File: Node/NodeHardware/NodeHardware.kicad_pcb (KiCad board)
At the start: 2 copper layers, 100 x 100 mm, 83 parts, among them J1 USB_C_Receptacle_USB2.0_16P, Q1 AO3401A, Q2 AO3401A, U1 TPS565201DDCR, U2 TPS565201DDCR, U3 CH340C, U4 TLV70433DBVR, U5 MCP73831-2-OT, U6 UCC27511ADBV, U7 ESP32-S3-WROOM-1

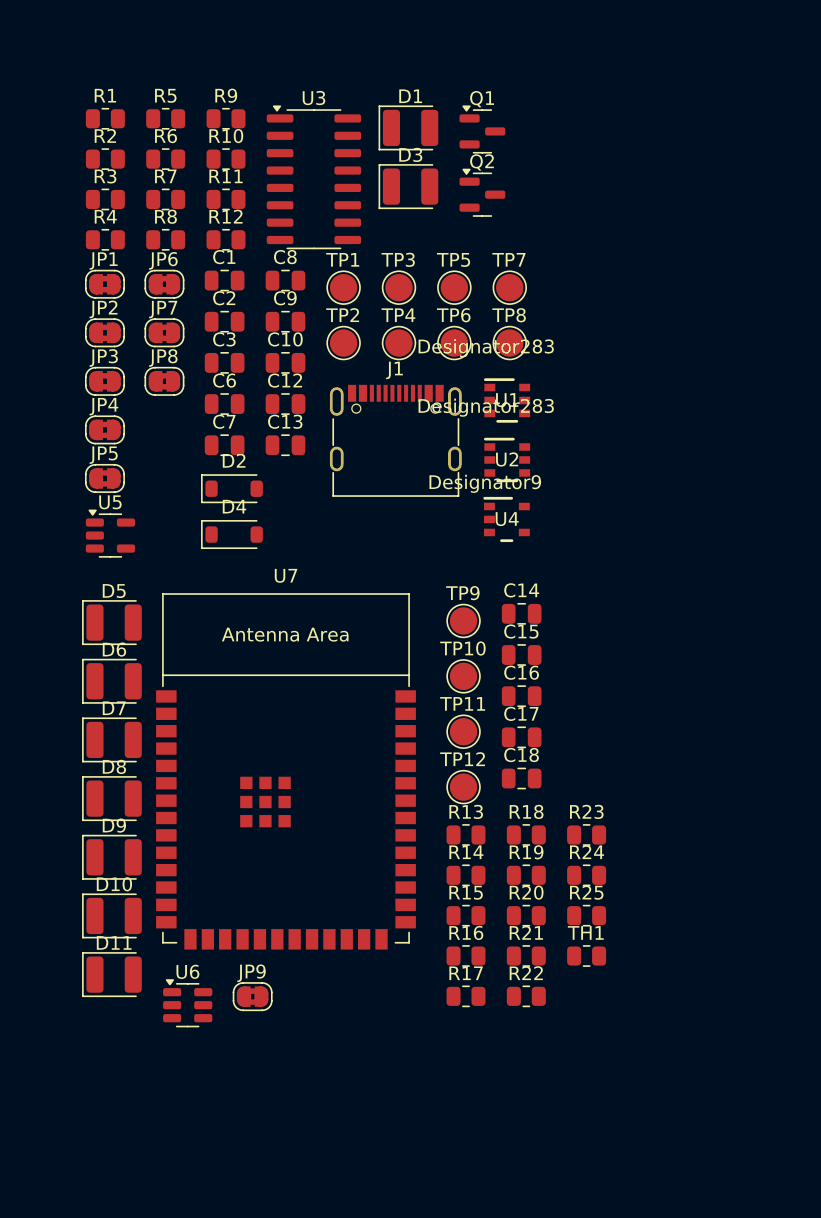
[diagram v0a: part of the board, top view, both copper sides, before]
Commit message: Finish all the basic SCHM needed for the ESP32
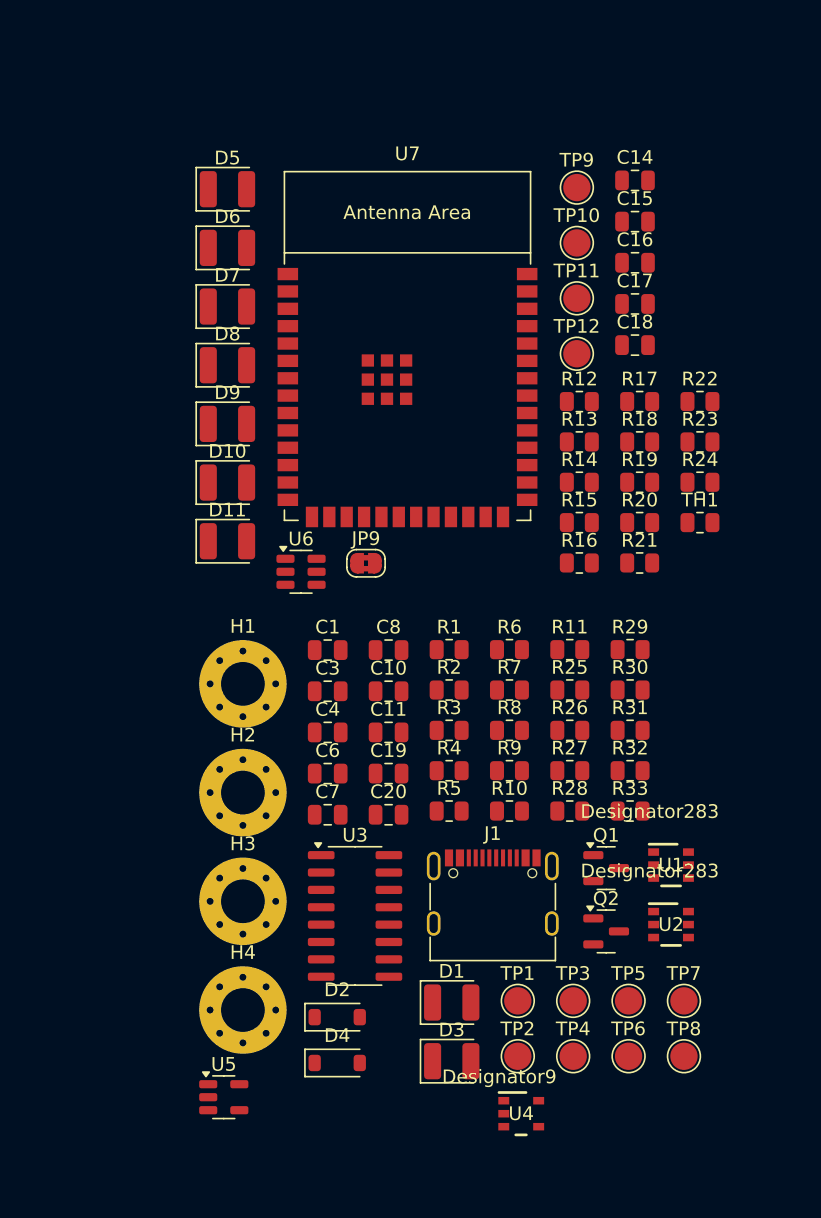
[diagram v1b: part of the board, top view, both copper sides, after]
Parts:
- removed C12, C13, C2, C9: C, Capacitor_SMD:C_0805_2012Metric
- removed JP1, JP2, JP3, JP4, JP5, JP6, JP7, JP8: SolderJumper_2_Bridged, Jumper:SolderJumper-2_P1.3mm_Bridged2Bar_RoundedPad1.0x1.5mm
- added C11: 1u, Capacitor_SMD:C_0805_2012Metric, F.Cu at (144.9, 104.5)
- added C19: 1u, Capacitor_SMD:C_0805_2012Metric, F.Cu at (144.9, 107.5)
- added C20: 100n, Capacitor_SMD:C_0805_2012Metric, F.Cu at (144.9, 110.5)
- added C4: 1u, Capacitor_SMD:C_0805_2012Metric, F.Cu at (140.4, 104.5)
- added H1: MountingHole, MountingHole:MountingHole_3.2mm_M3_Pad_Via, F.Cu at (134.2, 101.0)
- added H2: MountingHole, MountingHole:MountingHole_3.2mm_M3_Pad_Via, F.Cu at (134.2, 108.9)
- added H3: MountingHole, MountingHole:MountingHole_3.2mm_M3_Pad_Via, F.Cu at (134.2, 116.9)
- added H4: MountingHole, MountingHole:MountingHole_3.2mm_M3_Pad_Via, F.Cu at (134.2, 124.8)
- added R26: 0R, Resistor_SMD:R_0805_2012Metric, F.Cu at (158.2, 104.4)
- added R27: 4k7, Resistor_SMD:R_0805_2012Metric, F.Cu at (158.2, 107.3)
- added R28: 0R, Resistor_SMD:R_0805_2012Metric, F.Cu at (158.2, 110.3)
- added R29: 10k, Resistor_SMD:R_0805_2012Metric, F.Cu at (162.6, 98.5)
- added R30: 0R, Resistor_SMD:R_0805_2012Metric, F.Cu at (162.6, 101.4)
- added R31: 0R, Resistor_SMD:R_0805_2012Metric, F.Cu at (162.6, 104.4)
- added R32: 0R, Resistor_SMD:R_0805_2012Metric, F.Cu at (162.6, 107.3)
- added R33: 0R, Resistor_SMD:R_0805_2012Metric, F.Cu at (162.6, 110.3)
- C1, C8: value C -> 100n
- C10, C3, C6: value C -> 10u
- C7: value C -> 1u
- J1: value USB_C_Receptacle_USB2.0_16P -> USB_C_Receptacle_16P
- R1, R4, R9: value R -> 10k
- R10, R11: value R -> 5k1
- R12, R13, R14, R15, R16, R17, R18, R19, R20, R21, R22, R23, R24, R5, R8: value R -> 47k
- R2: value R -> 54.9k
- R25, R3: value R -> 0R
- R6: value R -> ???
- R7: value R -> 4k7
- TP1: value TestPoint -> 5V_TP
- TP2: value TestPoint -> V_IN_TP
- TP3: value TestPoint -> GND_TP_1
- TP4: value TestPoint -> GND_TP_2
- TP5: value TestPoint -> GND_TP_3
- TP6: value TestPoint -> GND_TP_4
- TP7: value TestPoint -> 3V3_TP
- moved D3 64.0 mm to (149.5, 128.6)
- moved D1 64.0 mm to (149.5, 124.3)
- moved R5 54.7 mm to (149.3, 110.3)
- moved Q1 54.6 mm to (160.8, 114.4)
- moved Q2 54.6 mm to (160.8, 119.1)
- moved U3 54.0 mm to (142.4, 117.9)
- moved TP3 53.7 mm to (158.4, 124.2)
- moved TP7 53.7 mm to (166.5, 124.2)
- moved TP1 53.7 mm to (154.3, 124.2)
- moved TP5 53.7 mm to (162.4, 124.2)
- moved TP2 53.7 mm to (154.3, 128.2)
- moved TP4 53.7 mm to (158.4, 128.2)
- moved TP6 53.7 mm to (162.4, 128.2)
- moved TP8 53.7 mm to (166.5, 128.2)
- moved R10 52.0 mm to (153.7, 110.3)
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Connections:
- net Net-(J1-D+-PadA6) renamed USB_D+
- net Net-(J1-D--PadA7) renamed USB_D-
- C1 pad 1: unconnected-(C1-Pad1) -> /5V_REG_SW
- C1 pad 2: unconnected-(C1-Pad2) -> Net-(U1-VBST)
- C10 pad 1: unconnected-(C10-Pad1) -> +3.3V
- C10 pad 2: unconnected-(C10-Pad2) -> PWR_IN_N
- C14 pad 1: GND -> PWR_IN_N
- C15 pad 1: GND -> PWR_IN_N
- C16 pad 1: GND -> PWR_IN_N
- C3 pad 1: unconnected-(C3-Pad1) -> +5V
- C3 pad 2: unconnected-(C3-Pad2) -> PWR_IN_N
- C6 pad 1: unconnected-(C6-Pad1) -> V_IN
- C6 pad 2: unconnected-(C6-Pad2) -> PWR_IN_N
- C7 pad 1: unconnected-(C7-Pad1) -> V_IN
- C7 pad 2: unconnected-(C7-Pad2) -> PWR_IN_N
- C8 pad 1: unconnected-(C8-Pad1) -> /3V3_REG_SW
- C8 pad 2: unconnected-(C8-Pad2) -> Net-(U2-VBST)
- D1 pad 1: unconnected-(D1-K-Pad1) -> /5V_REG_LED_K
- D1 pad 2: unconnected-(D1-A-Pad2) -> +5V
- D2 pad 1: unconnected-(D2-K-Pad1) -> V_IN
- D2 pad 2: unconnected-(D2-A-Pad2) -> /PWR_IN_ZENER
- D3 pad 1: unconnected-(D3-K-Pad1) -> /3V3_REG_LED_K
- D3 pad 2: unconnected-(D3-A-Pad2) -> +3.3V
- J1 pad A1: Net-(J1-GND-PadA1) -> PWR_IN_N
- J1 pad A12: Net-(J1-GND-PadA1) -> PWR_IN_N
- J1 pad A4: Net-(J1-VBUS-PadA4) -> VBUS
- J1 pad A5: unconnected-(J1-CC1-PadA5) -> Net-(J1-CC1)
- J1 pad A9: Net-(J1-VBUS-PadA4) -> VBUS
- J1 pad B1: Net-(J1-GND-PadA1) -> PWR_IN_N
- J1 pad B12: Net-(J1-GND-PadA1) -> PWR_IN_N
- J1 pad B4: Net-(J1-VBUS-PadA4) -> VBUS
- J1 pad B5: unconnected-(J1-CC2-PadB5) -> Net-(J1-CC2)
- J1 pad B9: Net-(J1-VBUS-PadA4) -> VBUS
- Q1 pad 1: unconnected-(Q1-G-Pad1) -> /PWR_IN_ZENER
- Q1 pad 2: unconnected-(Q1-S-Pad2) -> V_IN
- Q1 pad 3: unconnected-(Q1-D-Pad3) -> PWR_IN_P
- R1 pad 1: unconnected-(R1-Pad1) -> /5V_REG_IN
- R1 pad 2: unconnected-(R1-Pad2) -> 5V_REG_EN
- R10 pad 1: unconnected-(R10-Pad1) -> Net-(J1-CC1)
- R10 pad 2: unconnected-(R10-Pad2) -> PWR_IN_N
- R11 pad 1: unconnected-(R11-Pad1) -> Net-(J1-CC2)
- R11 pad 2: unconnected-(R11-Pad2) -> PWR_IN_N
- R13 pad 1: +BATT -> +3.3V
- R14 pad 1: +3.3V -> +BATT
- R16 pad 1: Net-(R13-Pad2) -> Net-(R14-Pad2)
- R16 pad 2: GND -> PWR_IN_N
- R2 pad 1: unconnected-(R2-Pad1) -> +5V
- R2 pad 2: unconnected-(R2-Pad2) -> /5V_REG_VFB
- R25 pad 1: unconnected-(R25-Pad1) -> +5V
- R25 pad 2: unconnected-(R25-Pad2) -> /3V3_REG_IN
- R3 pad 1: unconnected-(R3-Pad1) -> VBUS
- R3 pad 2: unconnected-(R3-Pad2) -> +5V
- R4 pad 1: unconnected-(R4-Pad1) -> /5V_REG_VFB
- R4 pad 2: unconnected-(R4-Pad2) -> PWR_IN_N
- R5 pad 1: unconnected-(R5-Pad1) -> /PWR_IN_ZENER
- R5 pad 2: unconnected-(R5-Pad2) -> PWR_IN_N
- R6 pad 1: unconnected-(R6-Pad1) -> +3.3V
- R6 pad 2: unconnected-(R6-Pad2) -> /3V3_REG_VFB
- R7 pad 1: unconnected-(R7-Pad1) -> /3V3_REG_LED_K
- R7 pad 2: unconnected-(R7-Pad2) -> PWR_IN_N
- R9 pad 1: unconnected-(R9-Pad1) -> /3V3_REG_VFB
- R9 pad 2: unconnected-(R9-Pad2) -> PWR_IN_N
- TH1 pad 1: Net-(R14-Pad2) -> Net-(R13-Pad2)
- TH1 pad 2: GND -> PWR_IN_N
- TP1 pad 1: unconnected-(TP1-Pad1) -> +5V
- TP2 pad 1: unconnected-(TP2-Pad1) -> V_IN
- TP3 pad 1: unconnected-(TP3-Pad1) -> PWR_IN_N
- TP4 pad 1: unconnected-(TP4-Pad1) -> PWR_IN_N
- TP5 pad 1: unconnected-(TP5-Pad1) -> PWR_IN_N
- TP6 pad 1: unconnected-(TP6-Pad1) -> PWR_IN_N
- TP7 pad 1: unconnected-(TP7-Pad1) -> +3.3V
- U1 pad 1: unconnected-(U1-GND-Pad1) -> PWR_IN_N
- U1 pad 2: unconnected-(U1-SW-Pad2) -> /5V_REG_SW
- U1 pad 3: unconnected-(U1-VIN-Pad3) -> /5V_REG_IN
- U1 pad 4: unconnected-(U1-VFB-Pad4) -> /5V_REG_VFB
- U1 pad 5: unconnected-(U1-EN-Pad5) -> 5V_REG_EN
- U1 pad 6: unconnected-(U1-VBST-Pad6) -> Net-(U1-VBST)
- U2 pad 1: unconnected-(U2-GND-Pad1) -> PWR_IN_N
- U2 pad 2: unconnected-(U2-SW-Pad2) -> /3V3_REG_SW
- U2 pad 3: unconnected-(U2-VIN-Pad3) -> /3V3_REG_IN
- U2 pad 4: unconnected-(U2-VFB-Pad4) -> /3V3_REG_VFB
- U2 pad 5: unconnected-(U2-EN-Pad5) -> 3V3_REG_EN
- U2 pad 6: unconnected-(U2-VBST-Pad6) -> Net-(U2-VBST)
- U3 pad 1: unconnected-(U3-GND-Pad1) -> PWR_IN_N
- U3 pad 5: unconnected-(U3-UD+-Pad5) -> /CH340_USB_D+
- U3 pad 6: unconnected-(U3-UD--Pad6) -> /CH340_USB_D-
- U7 pad 1: GND -> PWR_IN_N
- U7 pad 40: GND -> PWR_IN_N
- U7 pad 41: GND -> PWR_IN_N

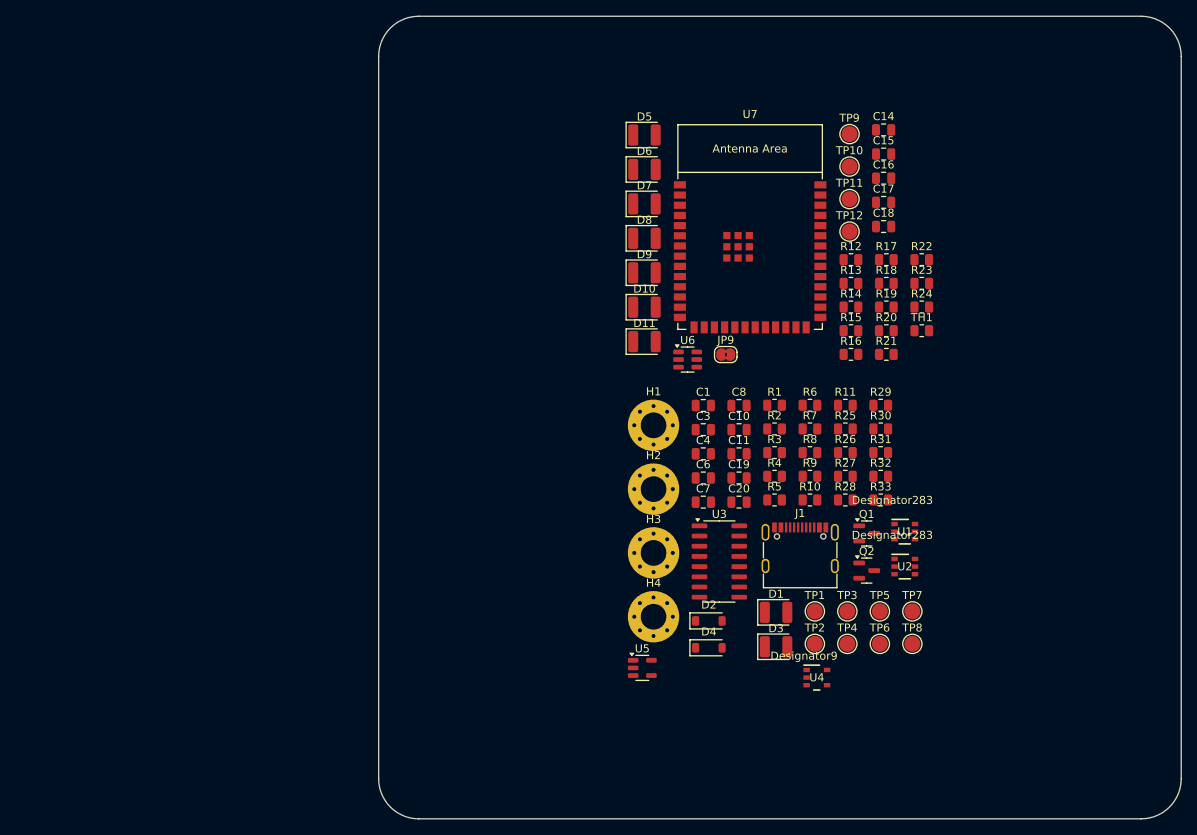
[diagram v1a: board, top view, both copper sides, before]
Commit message: added some comments and sim module to schematic
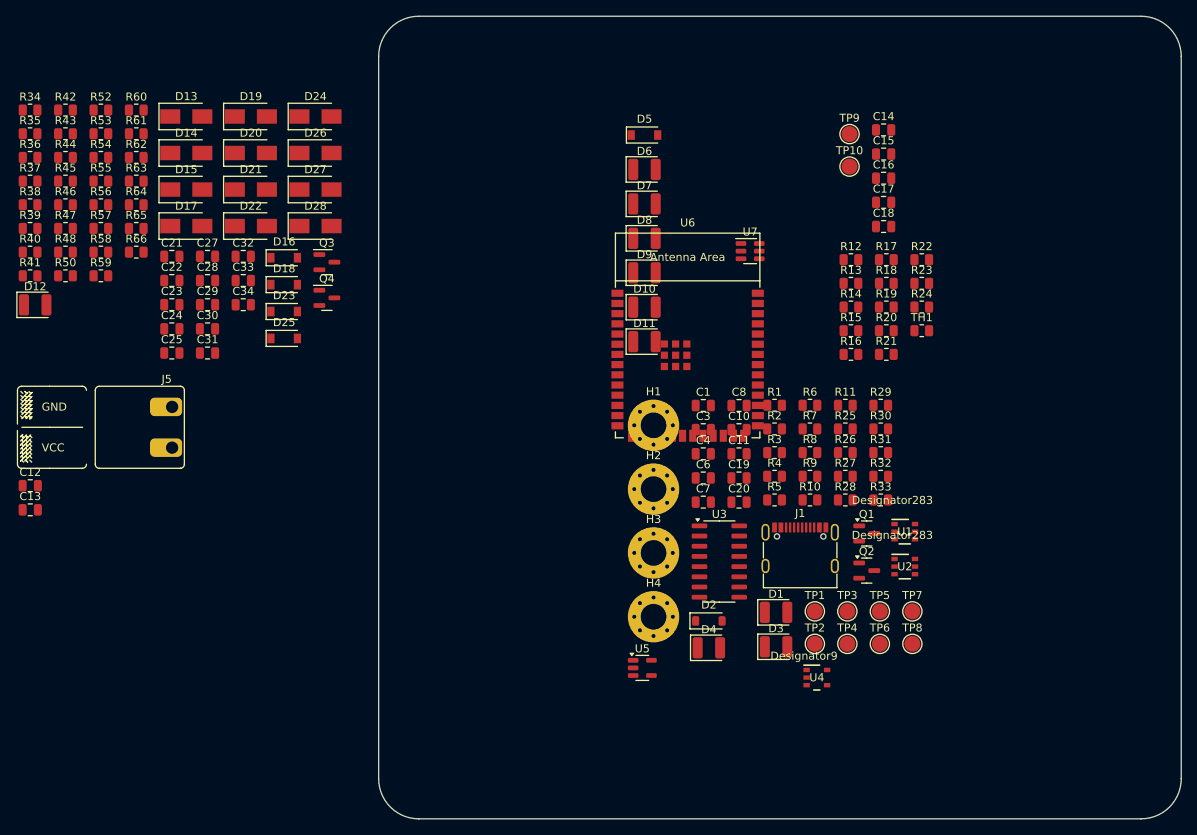
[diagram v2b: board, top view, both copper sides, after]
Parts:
- removed JP9: SolderJumper_2_Bridged, Jumper:SolderJumper-2_P1.3mm_Bridged2Bar_RoundedPad1.0x1.5mm
- removed TP11, TP12: TestPoint, TestPoint:TestPoint_Pad_D2.0mm
- added C12: 100n, Capacitor_SMD:C_0805_2012Metric, F.Cu at (56.6, 108.5)
- added C13: 4u7, Capacitor_SMD:C_0805_2012Metric, F.Cu at (56.6, 111.5)
- added C21: C, Capacitor_SMD:C_0805_2012Metric, F.Cu at (74.2, 79.9)
- added C22: 100n, Capacitor_SMD:C_0805_2012Metric, F.Cu at (74.2, 82.9)
- added C23: 100n, Capacitor_SMD:C_0805_2012Metric, F.Cu at (74.2, 85.9)
- added C24: 100n, Capacitor_SMD:C_0805_2012Metric, F.Cu at (74.2, 89.0)
- added C25: 100n, Capacitor_SMD:C_0805_2012Metric, F.Cu at (74.2, 92.0)
- added C27: 100n, Capacitor_SMD:C_0805_2012Metric, F.Cu at (78.7, 79.9)
- added C28: 100n, Capacitor_SMD:C_0805_2012Metric, F.Cu at (78.7, 82.9)
- added C29: 100n, Capacitor_SMD:C_0805_2012Metric, F.Cu at (78.7, 85.9)
- added C30: 100n, Capacitor_SMD:C_0805_2012Metric, F.Cu at (78.7, 89.0)
- added C31: 100n, Capacitor_SMD:C_0805_2012Metric, F.Cu at (78.7, 92.0)
- added C32: 100n, Capacitor_SMD:C_0805_2012Metric, F.Cu at (83.1, 79.9)
- added C33: 100n, Capacitor_SMD:C_0805_2012Metric, F.Cu at (83.1, 82.9)
- added C34: 100n, Capacitor_SMD:C_0805_2012Metric, F.Cu at (83.1, 85.9)
- added D12: YELLOW, LED_SMD:LED_1210_3225Metric, F.Cu at (57.2, 86.0)
- added D13: SS34, Diode_SMD:D_SMA, F.Cu at (76.0, 62.5)
- added D14: SS34, Diode_SMD:D_SMA, F.Cu at (76.0, 67.0)
- added D15: SS34, Diode_SMD:D_SMA, F.Cu at (76.0, 71.6)
- added D16: 3V6, Diode_SMD:D_SOD-123, F.Cu at (88.2, 80.1)
- added D17: SS34, Diode_SMD:D_SMA, F.Cu at (76.0, 76.1)
- added D18: 3V6, Diode_SMD:D_SOD-123, F.Cu at (88.2, 83.4)
- added D19: SS34, Diode_SMD:D_SMA, F.Cu at (84.1, 62.5)
- added D20: SS34, Diode_SMD:D_SMA, F.Cu at (84.1, 67.0)
- added D21: SS34, Diode_SMD:D_SMA, F.Cu at (84.1, 71.6)
- added D22: SS34, Diode_SMD:D_SMA, F.Cu at (84.1, 76.1)
- added D23: 3V6, Diode_SMD:D_SOD-123, F.Cu at (88.2, 86.8)
- added D24: SS34, Diode_SMD:D_SMA, F.Cu at (92.1, 62.5)
- added D25: 3V6, Diode_SMD:D_SOD-123, F.Cu at (88.2, 90.1)
- added D26: SS34, Diode_SMD:D_SMA, F.Cu at (92.1, 67.0)
- added D27: SS34, Diode_SMD:D_SMA, F.Cu at (92.1, 71.6)
- added D28: SS34, Diode_SMD:D_SMA, F.Cu at (92.1, 76.1)
- added J5: BATT, fflori4nComponents:TerminalBlockRemovablex2_Silk, F.Cu at (75.8, 101.2)
- added Q3: 2N7002, Package_TO_SOT_SMD:SOT-23, F.Cu at (93.6, 80.6)
- added Q4: 2N7002, Package_TO_SOT_SMD:SOT-23, F.Cu at (93.6, 85.1)
- added R34: 2k2, Resistor_SMD:R_0805_2012Metric, F.Cu at (56.6, 61.7)
- added R35: 2k2, Resistor_SMD:R_0805_2012Metric, F.Cu at (56.6, 64.6)
- added R36: 2k2, Resistor_SMD:R_0805_2012Metric, F.Cu at (56.6, 67.6)
- added R37: 2k2, Resistor_SMD:R_0805_2012Metric, F.Cu at (56.6, 70.5)
- added R38: 10k, Resistor_SMD:R_0805_2012Metric, F.Cu at (56.6, 73.5)
- added R39: 10k, Resistor_SMD:R_0805_2012Metric, F.Cu at (56.6, 76.4)
- added R40: 10k, Resistor_SMD:R_0805_2012Metric, F.Cu at (56.6, 79.4)
- added R41: 2k2, Resistor_SMD:R_0805_2012Metric, F.Cu at (56.6, 82.3)
- added R42: 47k, Resistor_SMD:R_0805_2012Metric, F.Cu at (61.0, 61.7)
- added R43: 47k, Resistor_SMD:R_0805_2012Metric, F.Cu at (61.0, 64.6)
- added R44: 47k, Resistor_SMD:R_0805_2012Metric, F.Cu at (61.0, 67.6)
- added R45: 100R, Resistor_SMD:R_0805_2012Metric, F.Cu at (61.0, 70.5)
- added R46: 10k, Resistor_SMD:R_0805_2012Metric, F.Cu at (61.0, 73.5)
- added R47: 100R, Resistor_SMD:R_0805_2012Metric, F.Cu at (61.0, 76.4)
- added R48: 10k, Resistor_SMD:R_0805_2012Metric, F.Cu at (61.0, 79.4)
- added R50: 220k, Resistor_SMD:R_0805_2012Metric, F.Cu at (61.0, 82.3)
- added R52: 220k, Resistor_SMD:R_0805_2012Metric, F.Cu at (65.4, 61.7)
- added R53: 100R, Resistor_SMD:R_0805_2012Metric, F.Cu at (65.4, 64.6)
- added R54: 10k, Resistor_SMD:R_0805_2012Metric, F.Cu at (65.4, 67.6)
- added R55: 100R, Resistor_SMD:R_0805_2012Metric, F.Cu at (65.4, 70.5)
- added R56: 10k, Resistor_SMD:R_0805_2012Metric, F.Cu at (65.4, 73.5)
- added R57: 100R, Resistor_SMD:R_0805_2012Metric, F.Cu at (65.4, 76.4)
- added R58: 10k, Resistor_SMD:R_0805_2012Metric, F.Cu at (65.4, 79.4)
- added R59: 100R, Resistor_SMD:R_0805_2012Metric, F.Cu at (65.4, 82.3)
- added R60: 10k, Resistor_SMD:R_0805_2012Metric, F.Cu at (69.8, 61.7)
- added R61: 100k, Resistor_SMD:R_0805_2012Metric, F.Cu at (69.8, 64.6)
- added R62: 100k, Resistor_SMD:R_0805_2012Metric, F.Cu at (69.8, 67.6)
- added R63: 220k, Resistor_SMD:R_0805_2012Metric, F.Cu at (69.8, 70.5)
- added R64: 220k, Resistor_SMD:R_0805_2012Metric, F.Cu at (69.8, 73.5)
- added R65: 100k, Resistor_SMD:R_0805_2012Metric, F.Cu at (69.8, 76.4)
- added R66: 100k, Resistor_SMD:R_0805_2012Metric, F.Cu at (69.8, 79.4)
- C14, C17: value C -> 1u
- C15, C18: value C -> 100n
- C16: value C -> 4u7
- C19: value 1u -> C
- C20: value 100n -> C
- D10, D11, D8, D9: value LED -> YELLOW
- D4: value 5V1 -> BLUE; footprint Diode_SMD:D_SOD-123 -> LED_SMD:LED_1210_3225Metric
- D5: value LED -> 5V1; footprint LED_SMD:LED_1210_3225Metric -> Diode_SMD:D_SOD-123
- D6: value LED -> RED
- D7: value LED -> GREEN
- R1, R29: value 10k -> 0R
- R10: value 5k1 -> ???
- R11: value 5k1 -> INF
- R12: value 47k -> 4k7
- R13, R14, R17, R19, R20, R21, R22, R24, R8: value 47k -> 0R
- R15: value 47k -> 10k
- R16, R18: value 47k -> 5k1
- R2: value 54.9k -> 10k
- R23: value 47k -> 2k2
- R26: value 0R -> 47k
- R27: value 4k7 -> 47k
- R3: value 0R -> 54.9k
- R30, R31, R32, R33: value 0R -> 2k2
- R4: value 10k -> INF
- R6: value ??? -> 4k7
- R7: value 4k7 -> 10k
- TH1: value PCB_TEMP_NTC -> 10k
- TP1: value 5V_TP -> V_IN_TP
- TP2: value V_IN_TP -> 5V_TP
- TP8: value TestPoint -> 3V3_LP_TP
- U6: value UCC27511ADBV -> ESP32-S3-WROOM-1; footprint Package_TO_SOT_SMD:SOT-23-6 -> Espressif:ESP32-S3-WROOM-1
- U7: value ESP32-S3-WROOM-1 -> UCC27511ADBV; footprint Espressif:ESP32-S3-WROOM-1 -> Package_TO_SOT_SMD:SOT-23-6
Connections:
- C10 pad 1: +3.3V -> +3V3
- C10 pad 2: PWR_IN_N -> BATT_N
- C11 pad 1: +3.3V -> +3V3
- C11 pad 2: PWR_IN_N -> BATT_N
- C14 pad 1: PWR_IN_N -> +3V3_LP
- C14 pad 2: +3.3V -> BATT_N
- C15 pad 1: PWR_IN_N -> +BATT
- C15 pad 2: +3.3V -> BATT_N
- C16 pad 1: PWR_IN_N -> BATT_P
- C16 pad 2: +3.3V -> BATT_N
- C17 pad 1: unconnected-(C17-Pad1) -> BATT_N
- C17 pad 2: unconnected-(C17-Pad2) -> +3V3
- C18 pad 1: unconnected-(C18-Pad1) -> BATT_N
- C18 pad 2: unconnected-(C18-Pad2) -> +3V3
- C19 pad 1: unconnected-(C19-Pad1) -> JTAG_RST
- C19 pad 2: unconnected-(C19-Pad2) -> BATT_N
- C20 pad 1: unconnected-(C20-Pad1) -> BOOT
- C20 pad 2: unconnected-(C20-Pad2) -> BATT_N
- C3 pad 1: +5V -> V_IN
- C3 pad 2: PWR_IN_N -> BATT_N
- C4 pad 1: +5V -> V_IN
- C4 pad 2: PWR_IN_N -> BATT_N
- C6 pad 1: V_IN -> +5V
- C6 pad 2: PWR_IN_N -> BATT_N
- C7 pad 1: V_IN -> +5V
- C7 pad 2: PWR_IN_N -> BATT_N
- D10 pad 1: unconnected-(D10-K-Pad1) -> /MCU_And_Peripherals/SPI_MOSI_LED_K
- D10 pad 2: unconnected-(D10-A-Pad2) -> +3V3
- D11 pad 1: unconnected-(D11-K-Pad1) -> /MCU_And_Peripherals/SPI_MISO_LED_K
- D11 pad 2: unconnected-(D11-A-Pad2) -> +3V3
- D3 pad 2: +3.3V -> +3V3
- D4 pad 1: unconnected-(D4-K-Pad1) -> /BATT_LED_K
- D4 pad 2: unconnected-(D4-A-Pad2) -> Net-(D4-A)
- D5 pad 1: unconnected-(D5-K-Pad1) -> +BATT
- D5 pad 2: unconnected-(D5-A-Pad2) -> /BATT_IN_ZENER
- D6 pad 1: unconnected-(D6-K-Pad1) -> /MCU_And_Peripherals/LED_01_K
- D6 pad 2: unconnected-(D6-A-Pad2) -> LED_01
- D7 pad 1: unconnected-(D7-K-Pad1) -> /MCU_And_Peripherals/LED_02_K
- D7 pad 2: unconnected-(D7-A-Pad2) -> LED_02
- D8 pad 1: unconnected-(D8-K-Pad1) -> /MCU_And_Peripherals/UART_RX_LED_K
- D8 pad 2: unconnected-(D8-A-Pad2) -> +3V3
- D9 pad 1: unconnected-(D9-K-Pad1) -> /MCU_And_Peripherals/UART_TX_LED_K
- D9 pad 2: unconnected-(D9-A-Pad2) -> +3V3
- H1 pad 1: PWR_IN_N -> BATT_N
- H2 pad 1: PWR_IN_N -> BATT_N
- H3 pad 1: PWR_IN_N -> BATT_N
- H4 pad 1: PWR_IN_N -> BATT_N
- J1 pad A1: PWR_IN_N -> BATT_N
- J1 pad A12: PWR_IN_N -> BATT_N
- J1 pad B1: PWR_IN_N -> BATT_N
- J1 pad B12: PWR_IN_N -> BATT_N
- Q2 pad 1: unconnected-(Q2-G-Pad1) -> /BATT_IN_ZENER
- Q2 pad 2: unconnected-(Q2-S-Pad2) -> +BATT
- Q2 pad 3: unconnected-(Q2-D-Pad3) -> BATT_P
- R1 pad 1: /5V_REG_IN -> V_IN
- R1 pad 2: 5V_REG_EN -> /5V_REG_IN
- R10 pad 1: Net-(J1-CC1) -> +3V3
- R10 pad 2: PWR_IN_N -> /3V3_REG_VFB
- R11 pad 1: Net-(J1-CC2) -> BATT_N
- R11 pad 2: PWR_IN_N -> 3V3_REG_EN
- R12 pad 1: unconnected-(R12-Pad1) -> /3V3_REG_LED_K
- R12 pad 2: unconnected-(R12-Pad2) -> BATT_N
- R13 pad 1: +3.3V -> +3V3
- R13 pad 2: Net-(R13-Pad2) -> Net-(U3-V3)
- R14 pad 1: +BATT -> VBUS
- R14 pad 2: Net-(R14-Pad2) -> +5V
- R15 pad 1: unconnected-(R15-Pad1) -> /3V3_REG_VFB
- R15 pad 2: unconnected-(R15-Pad2) -> BATT_N
- R16 pad 1: Net-(R14-Pad2) -> Net-(J1-CC1)
- R16 pad 2: PWR_IN_N -> BATT_N
- R17 pad 1: unconnected-(R17-Pad1) -> /net_lable
- R17 pad 2: unconnected-(R17-Pad2) -> UART_UC_RX
- R18 pad 1: unconnected-(R18-Pad1) -> Net-(J1-CC2)
- R18 pad 2: unconnected-(R18-Pad2) -> BATT_N
- R19 pad 1: unconnected-(R19-Pad1) -> /net_lable
- R19 pad 2: unconnected-(R19-Pad2) -> UART_UC_TX
- R2 pad 1: +5V -> /5V_REG_IN
- R2 pad 2: /5V_REG_VFB -> 5V_REG_EN
- R20 pad 1: unconnected-(R20-Pad1) -> USB_D+
- R20 pad 2: unconnected-(R20-Pad2) -> /CH340_USB_D+
- R21 pad 1: unconnected-(R21-Pad1) -> USB_D-
- R21 pad 2: unconnected-(R21-Pad2) -> /CH340_USB_D-
- R22 pad 1: unconnected-(R22-Pad1) -> Net-(D4-A)
- R22 pad 2: unconnected-(R22-Pad2) -> +5V
- R23 pad 1: unconnected-(R23-Pad1) -> Net-(U5-STAT)
- R23 pad 2: unconnected-(R23-Pad2) -> /BATT_LED_K
- R24 pad 1: unconnected-(R24-Pad1) -> +BATT
- R24 pad 2: unconnected-(R24-Pad2) -> /3V3_LP_REG_IN
- R25 pad 1: +5V -> Net-(U5-PROG)
- R25 pad 2: /3V3_REG_IN -> Net-(R25-Pad2)
- R26 pad 1: V_IN -> /BATT_IN_ZENER
- R26 pad 2: /5V_REG_IN -> BATT_N
- R27 pad 1: /5V_REG_LED_K -> Net-(R25-Pad2)
- R27 pad 2: PWR_IN_N -> BATT_N
- R28 pad 1: unconnected-(R28-Pad1) -> USB_D+
- R28 pad 2: unconnected-(R28-Pad2) -> Net-(U6-GPIO20/U1CTS/ADC2_CH9/CLK_OUT1/USB_D+)
- R29 pad 1: /3V3_REG_IN -> USB_D-
- R29 pad 2: 3V3_REG_EN -> Net-(U6-GPIO19/U1RTS/ADC2_CH8/CLK_OUT2/USB_D-)
- R3 pad 1: VBUS -> +5V
- R3 pad 2: +5V -> /5V_REG_VFB
- R30 pad 1: USB_D+ -> /MCU_And_Peripherals/LED_01_K
- R30 pad 2: /CH340_USB_D+ -> BATT_N
- R31 pad 1: USB_D- -> /MCU_And_Peripherals/LED_02_K
- R31 pad 2: /CH340_USB_D- -> BATT_N
- R32 pad 1: unconnected-(R32-Pad1) -> /MCU_And_Peripherals/UART_RX_LED_K
- R32 pad 2: unconnected-(R32-Pad2) -> UART_UC_RX
- R33 pad 1: unconnected-(R33-Pad1) -> /MCU_And_Peripherals/UART_TX_LED_K
- R33 pad 2: unconnected-(R33-Pad2) -> UART_UC_TX
- R4 pad 1: /5V_REG_VFB -> BATT_N
- R4 pad 2: PWR_IN_N -> 5V_REG_EN
- R5 pad 2: PWR_IN_N -> BATT_N
- R6 pad 1: +3.3V -> /5V_REG_LED_K
- R6 pad 2: /3V3_REG_VFB -> BATT_N
- R7 pad 1: /3V3_REG_LED_K -> /5V_REG_VFB
- R7 pad 2: PWR_IN_N -> BATT_N
- R8 pad 1: unconnected-(R8-Pad1) -> +5V
- R8 pad 2: unconnected-(R8-Pad2) -> /3V3_REG_IN
- R9 pad 1: /3V3_REG_VFB -> /3V3_REG_IN
- R9 pad 2: PWR_IN_N -> 3V3_REG_EN
- TH1 pad 1: Net-(R13-Pad2) -> PCB_TEMP
- TH1 pad 2: PWR_IN_N -> BATT_N
- TP1 pad 1: +5V -> V_IN
- TP10 pad 1: unconnected-(TP10-Pad1) -> LED_02
- TP2 pad 1: V_IN -> +5V
- TP3 pad 1: PWR_IN_N -> BATT_N
- TP4 pad 1: PWR_IN_N -> BATT_N
- TP5 pad 1: PWR_IN_N -> BATT_N
- TP6 pad 1: PWR_IN_N -> BATT_N
- TP7 pad 1: +3.3V -> +3V3
- TP8 pad 1: unconnected-(TP8-Pad1) -> +3V3_LP
- TP9 pad 1: unconnected-(TP9-Pad1) -> LED_01
- U1 pad 1: PWR_IN_N -> BATT_N
- U2 pad 1: PWR_IN_N -> BATT_N
- U3 pad 1: PWR_IN_N -> BATT_N
- U3 pad 13: unconnected-(U3-~{DTR}-Pad13) -> CH340_DTR
- U3 pad 14: unconnected-(U3-~{RTS}-Pad14) -> CH340_RTS
- U3 pad 16: unconnected-(U3-VCC-Pad16) -> Net-(U3-V3)
- U3 pad 2: unconnected-(U3-TXD-Pad2) -> /net_lable
- U3 pad 3: unconnected-(U3-RXD-Pad3) -> /net_lable
- U3 pad 4: unconnected-(U3-V3-Pad4) -> Net-(U3-V3)
- U4 pad 1: unconnected-(U4-GND-Pad1) -> BATT_N
- U4 pad 2: unconnected-(U4-IN-Pad2) -> /3V3_LP_REG_IN
- U4 pad 3: unconnected-(U4-OUT-Pad3) -> +3V3_LP
- U5 pad 1: unconnected-(U5-STAT-Pad1) -> Net-(U5-STAT)
- U5 pad 2: unconnected-(U5-V_{SS}-Pad2) -> BATT_N
- U5 pad 3: unconnected-(U5-V_{BAT}-Pad3) -> BATT_P
- U5 pad 4: unconnected-(U5-V_{DD}-Pad4) -> Net-(D4-A)
- U5 pad 5: unconnected-(U5-PROG-Pad5) -> Net-(U5-PROG)
- U6 pad 1: unconnected-(U6-V_{DD}-Pad1) -> BATT_N
- U6 pad 2: unconnected-(U6-OUTH-Pad2) -> +3V3
- U6 pad 3: unconnected-(U6-OUTL-Pad3) -> JTAG_RST
- U7 pad 1: PWR_IN_N -> unconnected-(U7-V_{DD}-Pad1)
- U7 pad 2: +3.3V -> unconnected-(U7-OUTH-Pad2)
